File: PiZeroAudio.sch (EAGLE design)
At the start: 53 parts, among them CN1 1X4-BIG, CON1 RPI-ZERO, J1 1X2-3.5MM, U3 NC7WZ16, U4 TPA3144D2PWPR

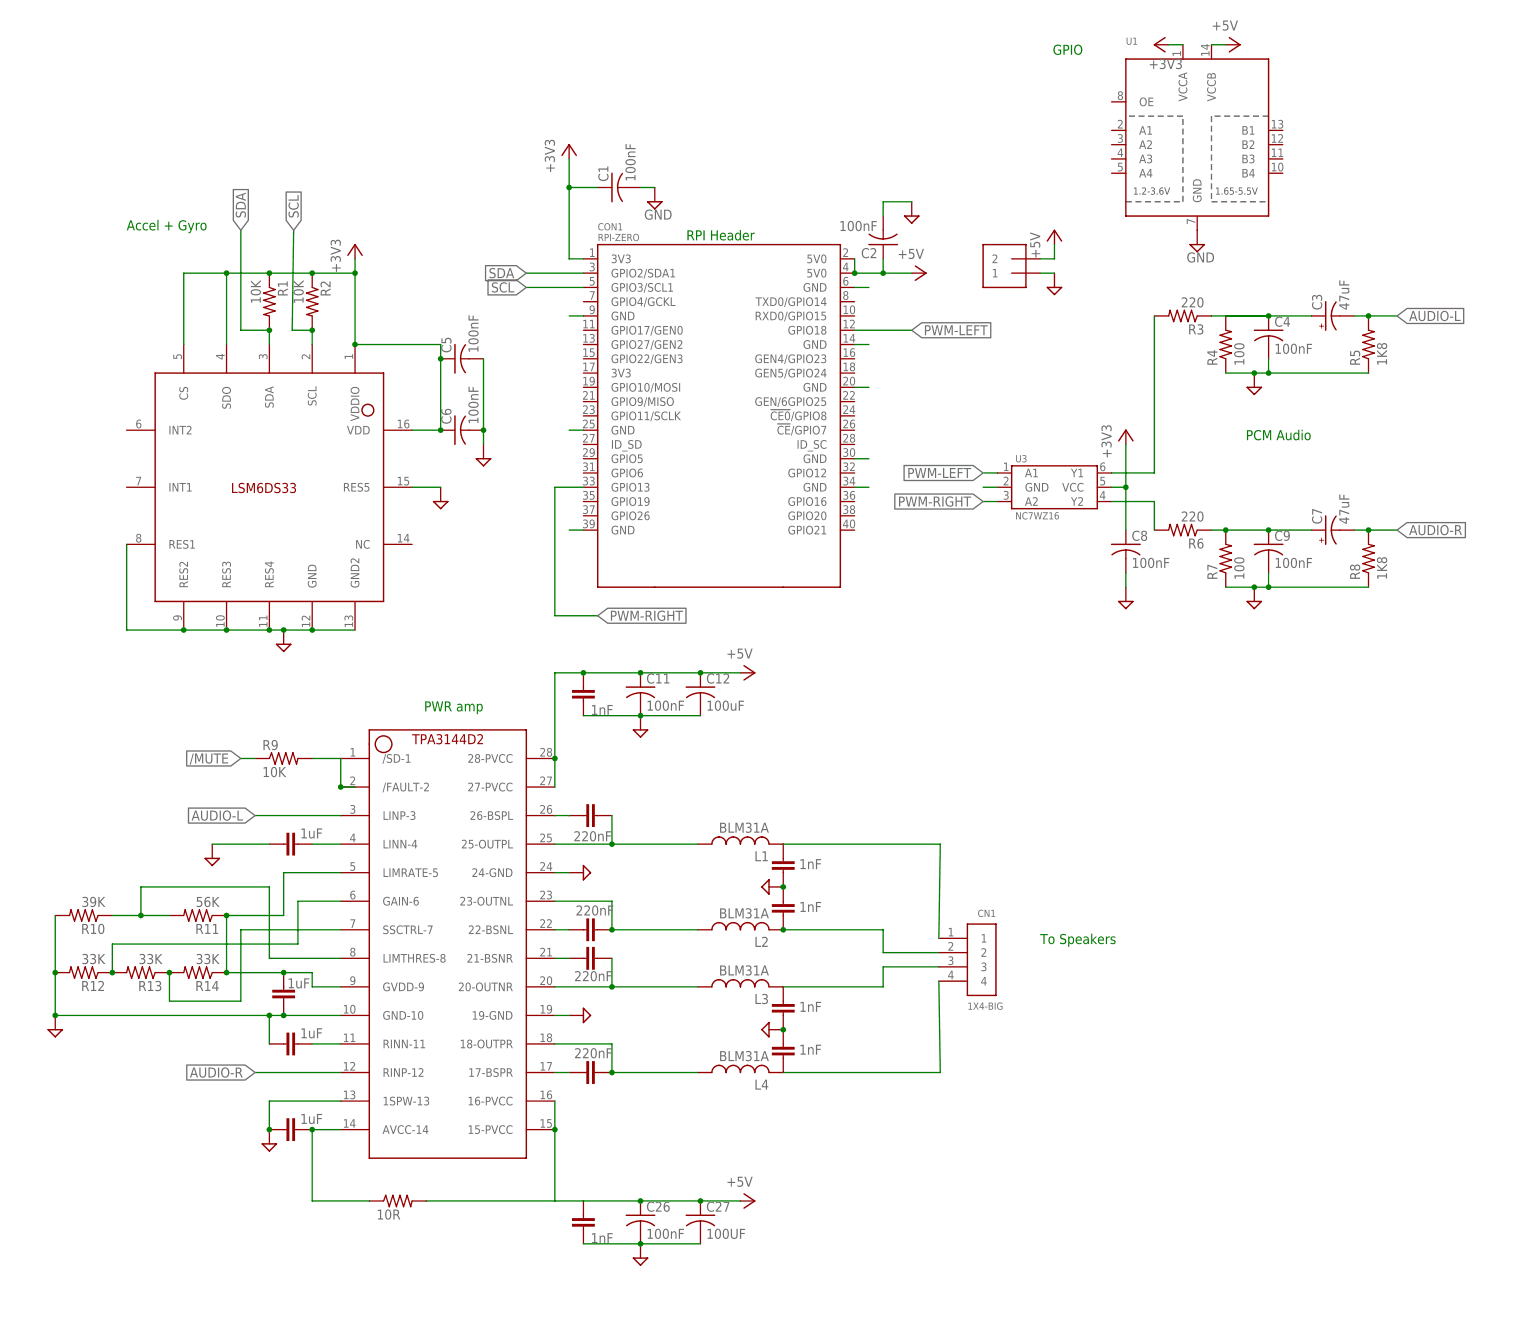
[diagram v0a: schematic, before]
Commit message: Renumbered Pins Placed components for first board
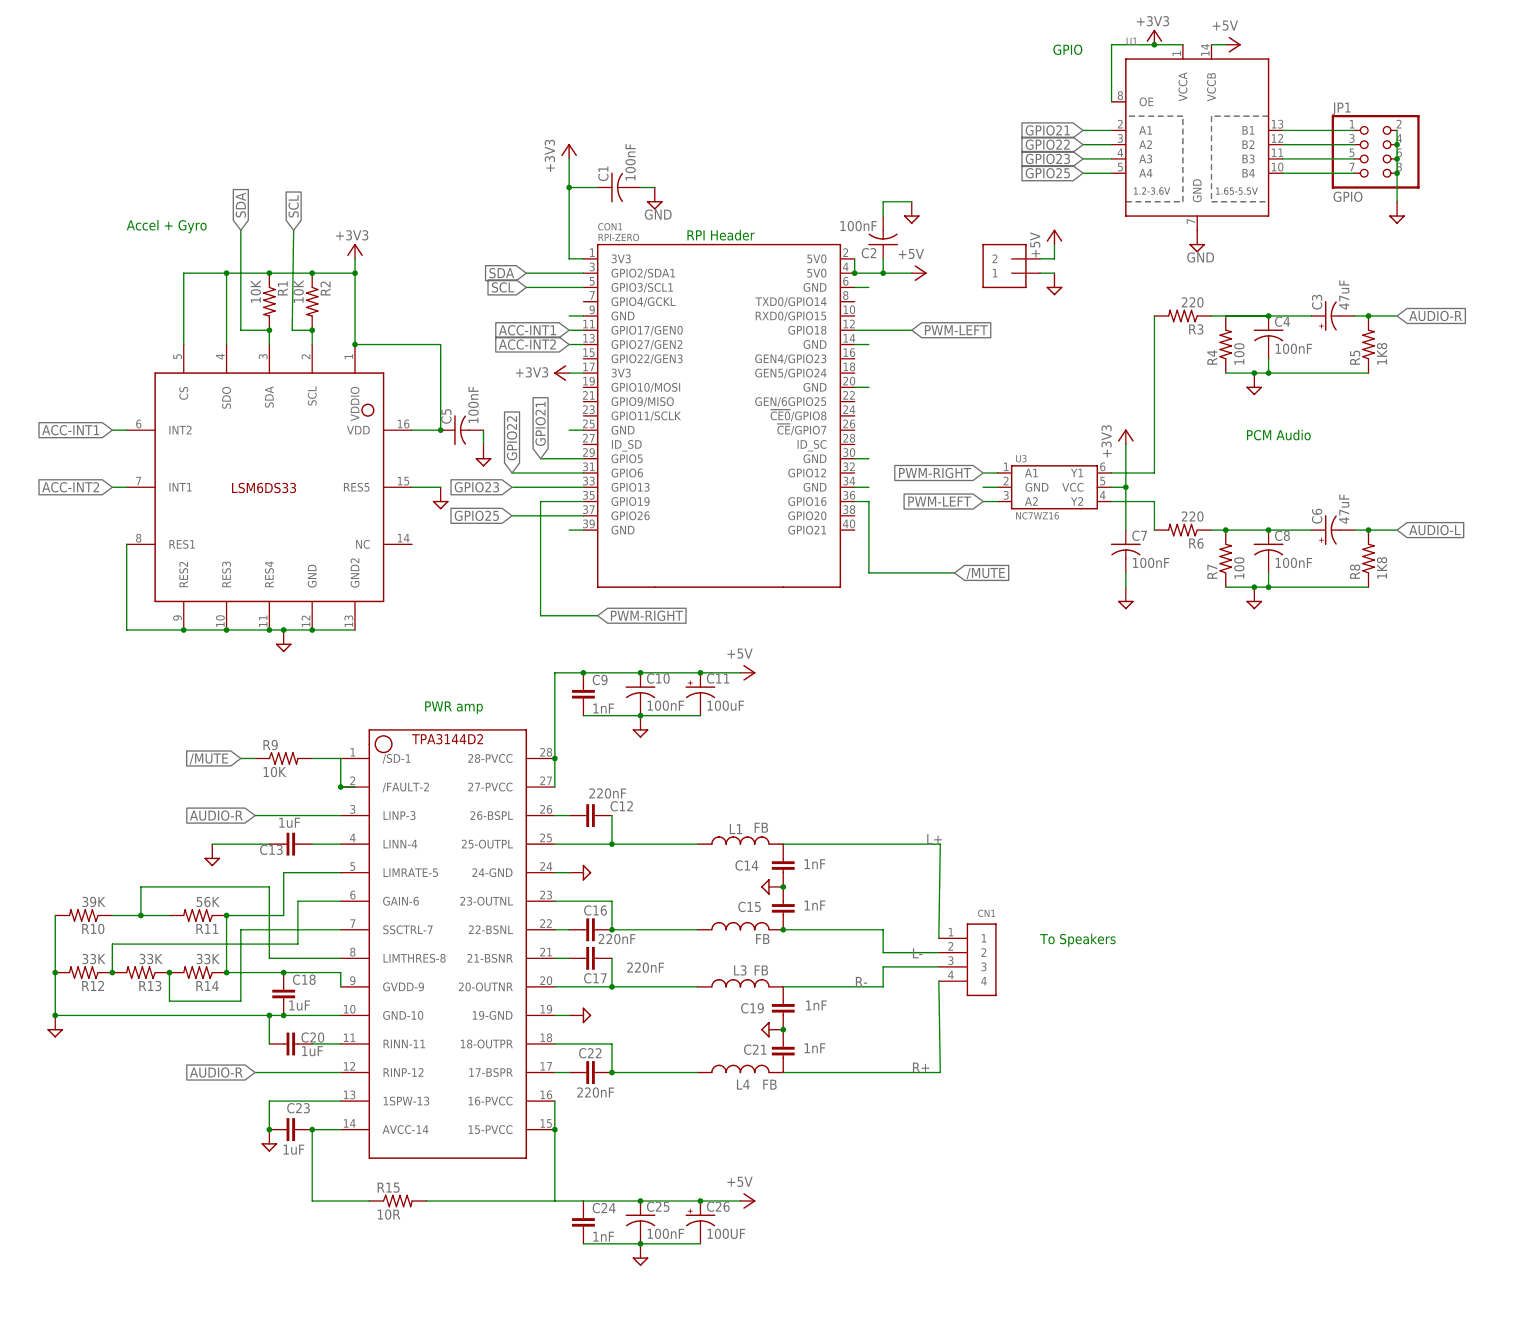
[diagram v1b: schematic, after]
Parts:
- removed C27: 100UF, adafruit:C-USC0805
- added JP1: GPIO, adafruit:PINHD-2X4
- C10, C25: value 1nF -> 100nF; device resistor:C-EUC0805 -> adafruit:C-USC0805
- C11: value 100nF -> 100uF; device adafruit:C-USC0805 -> adafruit:CPOL-USCT3528
- C12: value 100uF -> 220nF; device adafruit:C-USC0805 -> resistor:C-EUC0805
- C13, C18, C23: value 220nF -> 1uF
- C14, C19, C21, C24: value 1uF -> 1nF
- C16, C22: value 1nF -> 220nF
- C20: value 1nF -> 1uF
- C26: value 100nF -> 100UF; device adafruit:C-USC0805 -> adafruit:CPOL-USCT3528
- C3: device adafruit:CPOL-US085CS-1AR -> adafruit:CPOL-USCT3528
- C6: value 100nF -> 47uF; device adafruit:C-USC0805 -> adafruit:CPOL-USCT3528
- C7: value 47uF -> 100nF; device adafruit:CPOL-US085CS-1AR -> adafruit:C-USC0805
- C9: value 100nF -> 1nF; device adafruit:C-USC0805 -> resistor:C-EUC0805
- L1, L2, L3, L4: value BLM31A -> FB
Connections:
- new net ACC-INT1: CON1.GPIO17/GEN0, U2.INT2
- new net ACC-INT2: CON1.GPIO27/GEN2, U2.INT1
- new net GPIO21: CON1.GPIO5, U1.A1
- new net GPIO22: CON1.GPIO6, U1.A2
- new net GPIO23: CON1.GPIO13, U1.A3
- new net GPIO25: CON1.GPIO26, U1.A4
- new net L+: C14.1, CN1.1, L1.2
- new net L-: C15.2, CN1.2, L2.2
- new net R+: C21.2, CN1.4, L4.2
- new net R-: C19.1, CN1.3, L3.2
- net +3V3: now also C7.1, CON1.3V3@2, U1.OE; no longer C6.1, C8.1
- net +5V: now also C11.+, C24.1, C26.+, C9.1; no longer C11.1, C12.1, C26.1, C27.1
- net /MUTE: now also CON1.GPIO16
- net AUDIO-L: now also C6.-, R8.2; no longer C3.-, R5.2
- net AUDIO-R: now also C3.-, R5.2; no longer C7.-, R8.2
- net GND: now also C11.-, C13.2, C15.1, C18.2, C21.1, C23.2, C26.-, C7.2, JP1.2, JP1.4, JP1.6, JP1.8; no longer C11.2, C12.2, C15.2, C16.1, C21.2, C22.1, C26.2, C27.2, C6.2
- net N$10: now also C22.2; no longer C23.2
- net N$11: now also JP1.1, U1.B1; no longer C16.2, CN1.2, L2.2
- net N$12: now also JP1.3, U1.B2; no longer C15.1, CN1.1, L1.2
- net N$13: now also C17.2; no longer C18.2
- net N$14: now also JP1.5, U1.B3; no longer C20.1, CN1.3, L3.2
- net N$15: now also JP1.7, U1.B4; no longer C22.2, CN1.4, L4.2
- net N$16: now also C16.2; no longer C17.2
- net N$17: now also C12.2; no longer C13.2
- net N$18: now also C12.1; no longer C13.1
- net N$19: now also C16.1; no longer C17.1
- net N$20: now also C17.1; no longer C18.1
- net N$21: now also C22.1; no longer C23.1
- net N$26: now also C18.1; no longer C19.1
- net N$4: now also C6.+, C8.1; no longer C7.+, C9.1
- net N$7: now also C13.1; no longer C14.1
- net N$8: now also C20.1; no longer C21.1
- net N$9: now also C23.1; no longer C24.1
- net PWM-LEFT: now also U3.A2; no longer U3.A1
- net PWM-RIGHT: now also CON1.GPIO19, U3.A1; no longer CON1.GPIO13, U3.A2
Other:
- moved on the sheet: C12, C5, C8, C9

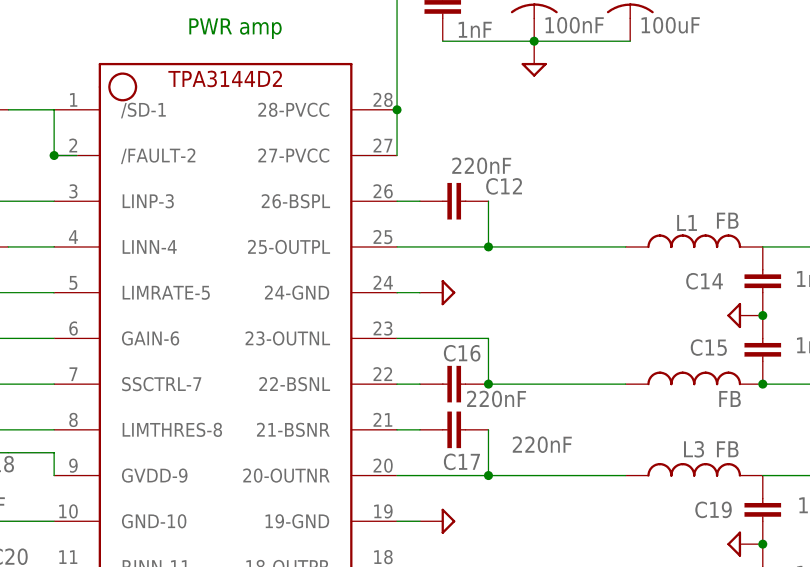
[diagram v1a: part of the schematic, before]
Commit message: Pre-resync board and schematic There is board inconsitency
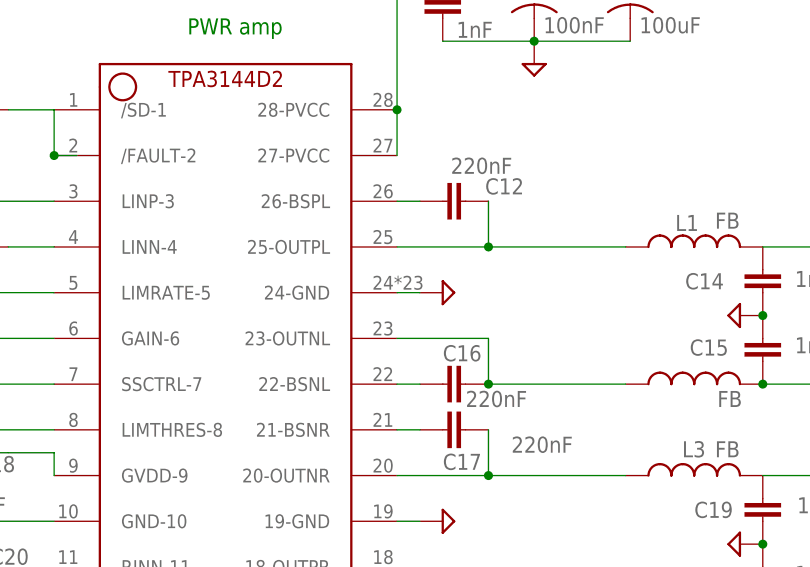
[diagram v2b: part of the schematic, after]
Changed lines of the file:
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@@
 </variantdefs>
 <classes>
-<class number="0" name="default" width="0" drill="0">
+<class number="0" name="default" width="0.1524" drill="0">
+<clearance class="0" value="0.1524"/>
+</class>
+<class number="2" name="PWM-LEFT" width="0.3048" drill="0.508">
+<clearance class="2" value="0.508"/>
+</class>
+<class number="3" name="PWM-RIGHT" width="0.3048" drill="0.508">
+<clearance class="3" value="0.508"/>
+</class>
+<class number="4" name="AUDIO-L" width="0.3048" drill="0.508">
+<clearance class="4" value="0.508"/>
+</class>
+<class number="5" name="AUDIO-R" width="0.3048" drill="0.508">
+<clearance class="5" value="0.508"/>
+</class>
+<class number="6" name="+5V" width="0.508" drill="0.508">
+<clearance class="6" value="0.254"/>
 </class>
 </classes>
